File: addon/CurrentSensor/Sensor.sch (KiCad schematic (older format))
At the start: 5 parts

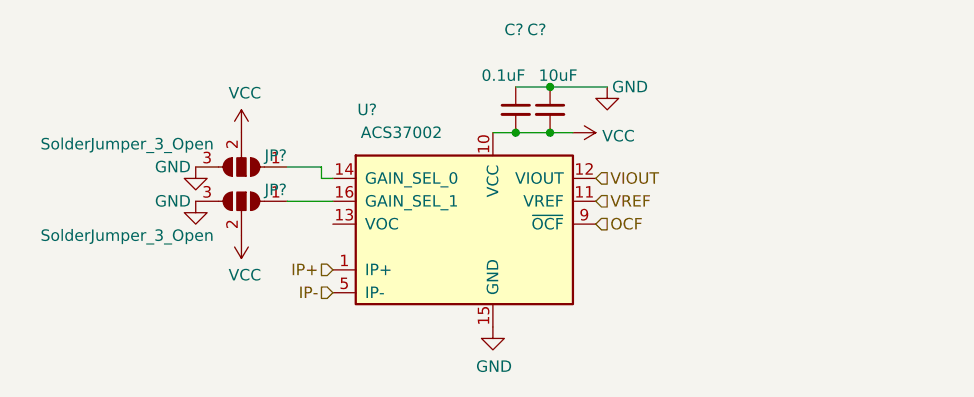
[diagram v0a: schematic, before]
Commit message: Fix power interconnects
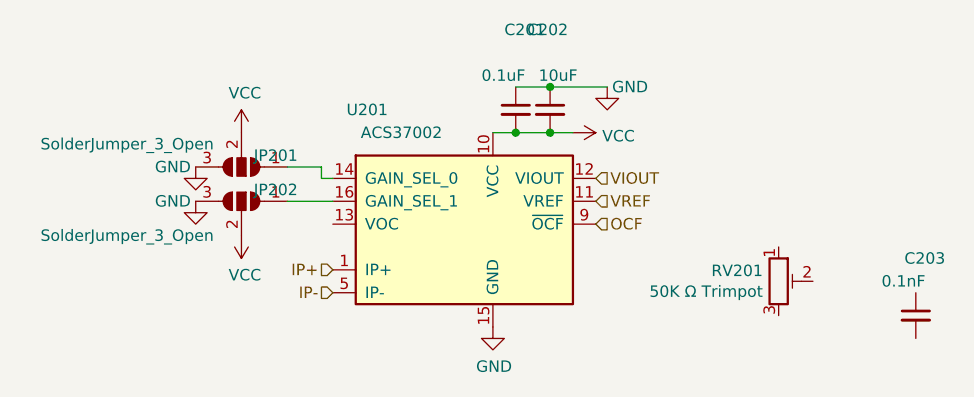
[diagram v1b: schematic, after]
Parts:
- added C203: 0.1nF, Capacitor_SMD:C_1206_3216Metric_Pad1.33x1.80mm_HandSolder, symbol Device:C_Small
- added RV201: 50K Ω Trimpot, Potentiometer_SMD:Potentiometer_Bourns_3214W_Vertical, symbol Device:R_Potentiometer_Trim
- JP201, JP202: renamed from JP?; footprint (none) -> Jumper:SolderJumper-3_P1.3mm_Open_RoundedPad1.0x1.5mm
- U201: renamed from U?; footprint (none) -> Package_SO:SOIC-16W_7.5x10.3mm_P1.27mm
- gave numbers to parts that had none: 2
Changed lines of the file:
@@
 	5150 3600 4950 3600
 $Comp
-L power:VCC #PWR?
+L power:VCC #PWR0101
 U 1 1 5FF5BAAE
 P 4750 3300
-F 0 "#PWR?" H 4750 3150 50  0001 C CNN
+AR Path="/5FF51AE2/5FF5BAAE" Ref="#PWR0101"  Part="1"
+AR Path="/5FF8E07D/5FF5BAAE" Ref="#PWR0108"  Part="1"
+F 0 "#PWR0101" H 4750 3150 50  0001 C CNN
 F 1 "VCC" H 4765 3473 50  0000 C CNN
 F 2 "" H 4750 3300 50  0001 C CNN
@@
 P 5450 3200
 AR Path="/5FF5267C" Ref="U?"  Part="1"
-AR Path="/5FF51AE2/5FF5267C" Ref="U?"  Part="1"
+AR Path="/5FF51AE2/5FF5267C" Ref="U201"  Part="1"
 AR Path="/5FF53ADE/5FF5267C" Ref="U?"  Part="1"
-F 0 "U?" H 5300 3200 50  0000 C CNN
+AR Path="/5FF8E07D/5FF5267C" Ref="U301"  Part="1"
+F 0 "U201" H 5300 3200 50  0000 C CNN
 F 1 "ACS37002" H 5450 3100 50  0000 C CNN
-F 2 "" H 5350 3250 50  0001 C CNN
-F 3 "" H 5350 3250 50  0001 C CNN
+F 2 "Package_SO:SOIC-16W_7.5x10.3mm_P1.27mm" H 5350 3250 50  0001 C CNN
+F 3 "https://www.allegromicro.com/-/media/files/datasheets/acs37002-datasheet.ashx" H 5350 3250 50  0001 C CNN
 	1    5450 3200
 	1    0    0    -1
 $EndComp
 $Comp
-L power:VCC #PWR?
+L power:VCC #PWR0102
 U 1 1 5FF5CE36
 P 6200 3300
-F 0 "#PWR?" H 6200 3150 50  0001 C CNN
+AR Path="/5FF51AE2/5FF5CE36" Ref="#PWR0102"  Part="1"
+AR Path="/5FF8E07D/5FF5CE36" Ref="#PWR0109"  Part="1"
+F 0 "#PWR0102" H 6200 3150 50  0001 C CNN
 F 1 "VCC" V 6215 3428 50  0000 L CNN
 F 2 "" H 6200 3300 50  0001 C CNN
@@
 $EndComp
 $Comp
-L power:GND #PWR?
+L power:GND #PWR0103
 U 1 1 5FF5D5F8
 P 5850 4150
-F 0 "#PWR?" H 5850 3900 50  0001 C CNN
+AR Path="/5FF51AE2/5FF5D5F8" Ref="#PWR0103"  Part="1"
+AR Path="/5FF8E07D/5FF5D5F8" Ref="#PWR0110"  Part="1"
+F 0 "#PWR0103" H 5850 3900 50  0001 C CNN
 F 1 "GND" H 5855 3977 50  0000 C CNN
 F 2 "" H 5850 4150 50  0001 C CNN
@@
 OCF
 $Comp
-L Jumper:SolderJumper_3_Open JP?
+L Jumper:SolderJumper_3_Open JP201
 U 1 1 5FF63253
 P 4750 3450
-F 0 "JP?" H 4600 3400 50  0000 C CNN
+AR Path="/5FF51AE2/5FF63253" Ref="JP201"  Part="1"
+AR Path="/5FF8E07D/5FF63253" Ref="JP301"  Part="1"
+F 0 "JP201" H 4600 3400 50  0000 C CNN
 F 1 "SolderJumper_3_Open" H 5250 3350 50  0000 C CNN
-F 2 "" H 4750 3450 50  0001 C CNN
+F 2 "Jumper:SolderJumper-3_P1.3mm_Open_RoundedPad1.0x1.5mm" H 4750 3450 50  0001 C CNN
 F 3 "~" H 4750 3450 50  0001 C CNN
 	1    4750 3450
@@
 $EndComp
 $Comp
-L power:GND #PWR?
+L power:GND #PWR0104
 U 1 1 5FF65EF6
 P 4550 3450
-F 0 "#PWR?" H 4550 3200 50  0001 C CNN
+AR Path="/5FF51AE2/5FF65EF6" Ref="#PWR0104"  Part="1"
+AR Path="/5FF8E07D/5FF65EF6" Ref="#PWR0111"  Part="1"
+F 0 "#PWR0104" H 4550 3200 50  0001 C CNN
 F 1 "GND" H 4450 3450 50  0000 C CNN
 F 2 "" H 4550 3450 50  0001 C CNN
@@
 $EndComp
 $Comp
-L power:VCC #PWR?
+L power:VCC #PWR0105
 U 1 1 5FF67C54
 P 4750 3750
-F 0 "#PWR?" H 4750 3600 50  0001 C CNN
+AR Path="/5FF51AE2/5FF67C54" Ref="#PWR0105"  Part="1"
+AR Path="/5FF8E07D/5FF67C54" Ref="#PWR0112"  Part="1"
+F 0 "#PWR0105" H 4750 3600 50  0001 C CNN
 F 1 "VCC" H 4765 3923 50  0000 C CNN
 F 2 "" H 4750 3750 50  0001 C CNN
@@
 $EndComp
 $Comp
-L Jumper:SolderJumper_3_Open JP?
+L Jumper:SolderJumper_3_Open JP202
 U 1 1 5FF67C5A
 P 4750 3600
-F 0 "JP?" H 4600 3650 50  0000 C CNN
+AR Path="/5FF51AE2/5FF67C5A" Ref="JP202"  Part="1"
+AR Path="/5FF8E07D/5FF67C5A" Ref="JP302"  Part="1"
+F 0 "JP202" H 4600 3650 50  0000 C CNN
 F 1 "SolderJumper_3_Open" H 5250 3450 50  0000 C CNN
-F 2 "" H 4750 3600 50  0001 C CNN
+F 2 "Jumper:SolderJumper-3_P1.3mm_Open_RoundedPad1.0x1.5mm" H 4750 3600 50  0001 C CNN
 F 3 "~" H 4750 3600 50  0001 C CNN
 	1    4750 3600
@@
 $EndComp
 $Comp
-L power:GND #PWR?
+L power:GND #PWR0106
 U 1 1 5FF67C60
 P 4550 3600
-F 0 "#PWR?" H 4550 3350 50  0001 C CNN
+AR Path="/5FF51AE2/5FF67C60" Ref="#PWR0106"  Part="1"
+AR Path="/5FF8E07D/5FF67C60" Ref="#PWR0113"  Part="1"
+F 0 "#PWR0106" H 4550 3350 50  0001 C CNN
 F 1 "GND" H 4650 3600 50  0000 C CNN
 F 2 "" H 4550 3600 50  0001 C CNN
@@
 $EndComp
 $Comp
-L Device:C_Small C?
+L Device:C_Small C201
 U 1 1 5FF7094C
 P 5950 3200
-F 0 "C?" H 5900 3550 50  0000 L CNN
+AR Path="/5FF51AE2/5FF7094C" Ref="C201"  Part="1"
+AR Path="/5FF8E07D/5FF7094C" Ref="C301"  Part="1"
+F 0 "C201" H 5900 3550 50  0000 L CNN
 F 1 "0.1uF" H 5800 3350 50  0000 L CNN
 F 2 "Capacitor_SMD:C_1206_3216Metric_Pad1.33x1.80mm_HandSolder" H 5950 3200 50  0001 C CNN
@@
 $EndComp
 $Comp
-L power:GND #PWR?
+L power:GND #PWR0107
 U 1 1 5FF77A0A
 P 6350 3100
-F 0 "#PWR?" H 6350 2850 50  0001 C CNN
+AR Path="/5FF51AE2/5FF77A0A" Ref="#PWR0107"  Part="1"
+AR Path="/5FF8E07D/5FF77A0A" Ref="#PWR0114"  Part="1"
+F 0 "#PWR0107" H 6350 2850 50  0001 C CNN
 F 1 "GND" H 6450 3100 50  0000 C CNN
 F 2 "" H 6350 3100 50  0001 C CNN
@@
 $EndComp
 $Comp
-L Device:C_Small C?
+L Device:C_Small C202
 U 1 1 5FF75051
 P 6100 3200
-F 0 "C?" H 6000 3550 50  0000 L CNN
+AR Path="/5FF51AE2/5FF75051" Ref="C202"  Part="1"
+AR Path="/5FF8E07D/5FF75051" Ref="C302"  Part="1"
+F 0 "C202" H 6000 3550 50  0000 L CNN
 F 1 "10uF" H 6050 3350 50  0000 L CNN
 F 2 "Capacitor_SMD:C_1206_3216Metric_Pad1.33x1.80mm_HandSolder" H 6100 3200 50  0001 C CNN
@@
 	6100 3300 6200 3300
 Connection ~ 6100 3300
+$Comp
+L Device:R_Potentiometer_Trim RV201
+U 1 1 5FF871BC
+P 7100 3950
+AR Path="/5FF51AE2/5FF871BC" Ref="RV201"  Part="1"
+AR Path="/5FF8E07D/5FF871BC" Ref="RV301"  Part="1"
+F 0 "RV201" H 7031 3996 50  0000 R CNN
+F 1 "50K Ω Trimpot" H 7031 3905 50  0000 R CNN
+F 2 "Potentiometer_SMD:Potentiometer_Bourns_3214W_Vertical" H 7100 3950 50  0001 C CNN
+F 3 "https://www.bourns.com/docs/Product-Datasheets/3214.pdf" H 7100 3950 50  0001 C CNN
+F 4 "3214X-1-503E" H 7100 3950 50  0001 C CNN "Model"
+F 5 "Bourns" H 7100 3950 50  0001 C CNN "Manufacturer"
+	1    7100 3950
+	1    0    0    -1
+$EndComp
+$Comp
+L Device:C_Small C203
+U 1 1 5FF8806D
+P 7700 4100
+AR Path="/5FF51AE2/5FF8806D" Ref="C203"  Part="1"
+AR Path="/5FF8E07D/5FF8806D" Ref="C303"  Part="1"
+F 0 "C203" H 7650 4350 50  0000 L CNN
+F 1 "0.1nF" H 7550 4250 50  0000 L CNN
+F 2 "Capacitor_SMD:C_1206_3216Metric_Pad1.33x1.80mm_HandSolder" H 7700 4100 50  0001 C CNN
+F 3 "https://api.kemet.com/component-edge/download/datasheet/C1206C104K4RACTU.pdf" H 7700 4100 50  0001 C CNN
+F 4 "Kemet" H 7700 4100 50  0001 C CNN "Manufacturer"
+F 5 "C1206C102K4RACTU" H 7700 4100 50  0001 C CNN "Model"
+	1    7700 4100
+	1    0    0    -1
+$EndComp
 $EndSCHEMATC
